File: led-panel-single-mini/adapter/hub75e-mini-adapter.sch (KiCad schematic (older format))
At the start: 2 parts, among them J1 Conn_02x08_Odd_Even, J2 Conn_02x08_Odd_Even

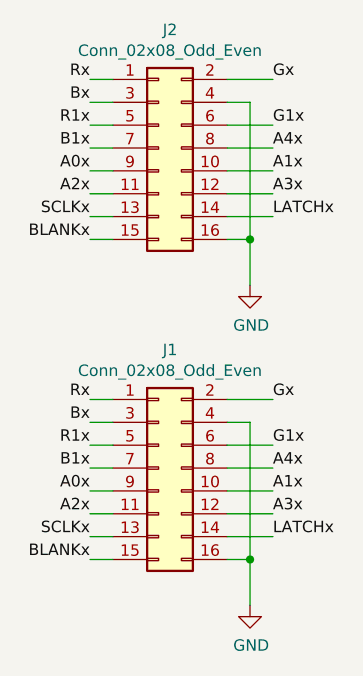
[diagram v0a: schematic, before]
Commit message: Corrected spacing and legend of the small led panel connector adapter.
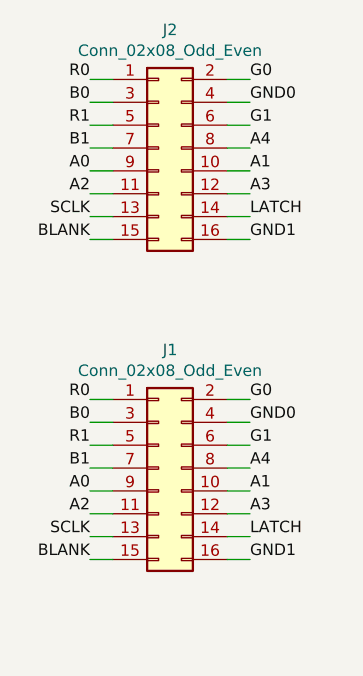
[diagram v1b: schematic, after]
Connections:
- net A0x renamed A0
- net A1x renamed A1
- net A2x renamed A2
- net A3x renamed A3
- net A4x renamed A4
- net B1x renamed B1
- net BLANKx renamed BLANK
- net Bx renamed B0
- net G1x renamed G1
- net GND renamed GND0
- net GND0: no longer J1.16 (Pin_16), J2.16 (Pin_16)
- net Gx renamed G0
- net LATCHx renamed LATCH
- net R1x renamed R1
- net Rx renamed R0
- net SCLKx renamed SCLK
- new net GND1: J1.16 (Pin_16), J2.16 (Pin_16)
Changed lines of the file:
@@
 EESchema Schematic File Version 4
 LIBS:hub75e-mini-adapter-cache
-EELAYER 26 0
+EELAYER 29 0
 EELAYER END
 $Descr A4 11693 8268
@@
 Title "HUB75E Mini Adapter"
 Date ""
-Rev "V1.0a"
+Rev "V1.0b"
 Comp "1BitSquared"
 Comment1 "2018-2019 (C) 1BitSquared <info@1bitsquared.com>"
@@
 	5500 3000 5400 3000
 Text Label 5400 2800 2    50   ~ 0
-Rx
-Text Label 6200 2800 0    50   ~ 0
-Gx
+R0
+Text Label 6100 2800 0    50   ~ 0
+G0
 Text Label 5400 2900 2    50   ~ 0
-Bx
+B0
 Text Label 5400 3000 2    50   ~ 0
-R1x
-Text Label 6200 3000 0    50   ~ 0
-G1x
+R1
+Text Label 6100 3000 0    50   ~ 0
+G1
 Text Label 5400 3100 2    50   ~ 0
-B1x
+B1
 Text Label 5400 3200 2    50   ~ 0
-A0x
-Text Label 6200 3200 0    50   ~ 0
-A1x
+A0
+Text Label 6100 3200 0    50   ~ 0
+A1
 Text Label 5400 3300 2    50   ~ 0
-A2x
-Text Label 6200 3300 0    50   ~ 0
-A3x
+A2
+Text Label 6100 3300 0    50   ~ 0
+A3
 Text Label 5400 3400 2    50   ~ 0
-SCLKx
-Text Label 6200 3400 0    50   ~ 0
-LATCHx
+SCLK
+Text Label 6100 3400 0    50   ~ 0
+LATCH
 Text Label 5400 3500 2    50   ~ 0
-BLANKx
-Text Label 6200 3100 0    50   ~ 0
-A4x
+BLANK
+Text Label 6100 3100 0    50   ~ 0
+A4
 Wire Wire Line
 	5400 3100 5500 3100
@@
 	5400 3500 5500 3500
 Wire Wire Line
-	6000 2800 6200 2800
+	6000 2800 6100 2800
 Wire Wire Line
-	6000 3000 6200 3000
+	6000 3000 6100 3000
 Wire Wire Line
-	6000 3100 6200 3100
+	6000 3100 6100 3100
 Wire Wire Line
-	6000 3200 6200 3200
+	6000 3200 6100 3200
 Wire Wire Line
-	6000 3300 6200 3300
+	6000 3300 6100 3300
 Wire Wire Line
-	6000 3400 6200 3400
+	6000 3400 6100 3400
 Wire Wire Line
 	6000 2900 6100 2900
-Wire Wire Line
-	6100 2900 6100 3500
-Wire Wire Line
-	6100 3500 6100 3700
-Connection ~ 6100 3500
-$Comp
-L power:GND #PWR03
-U 1 1 5C8CBF07
-P 6100 3700
-F 0 "#PWR03" H 6100 3450 50  0001 C CNN
-F 1 "GND" H 6105 3524 50  0000 C CNN
-F 2 "" H 6100 3700 50  0001 C CNN
-F 3 "" H 6100 3700 50  0001 C CNN
-	1    6100 3700
-	1    0    0    -1
-$EndComp
 $Comp
 L Connector_Generic:Conn_02x08_Odd_Even J1
@@
 	5500 4400 5400 4400
 Text Label 5400 4200 2    50   ~ 0
-Rx
-Text Label 6200 4200 0    50   ~ 0
-Gx
+R0
+Text Label 6100 4200 0    50   ~ 0
+G0
 Text Label 5400 4300 2    50   ~ 0
-Bx
+B0
 Text Label 5400 4400 2    50   ~ 0
-R1x
-Text Label 6200 4400 0    50   ~ 0
-G1x
+R1
+Text Label 6100 4400 0    50   ~ 0
+G1
 Text Label 5400 4500 2    50   ~ 0
-B1x
+B1
 Text Label 5400 4600 2    50   ~ 0
-A0x
-Text Label 6200 4600 0    50   ~ 0
-A1x
+A0
+Text Label 6100 4600 0    50   ~ 0
+A1
 Text Label 5400 4700 2    50   ~ 0
-A2x
-Text Label 6200 4700 0    50   ~ 0
-A3x
+A2
+Text Label 6100 4700 0    50   ~ 0
+A3
 Text Label 5400 4800 2    50   ~ 0
-SCLKx
-Text Label 6200 4800 0    50   ~ 0
-LATCHx
+SCLK
+Text Label 6100 4800 0    50   ~ 0
+LATCH
 Text Label 5400 4900 2    50   ~ 0
-BLANKx
-Text Label 6200 4500 0    50   ~ 0
-A4x
+BLANK
+Text Label 6100 4500 0    50   ~ 0
+A4
 Wire Wire Line
 	5400 4500 5500 4500
@@
 	5400 4900 5500 4900
 Wire Wire Line
-	6000 4200 6200 4200
+	6000 4200 6100 4200
 Wire Wire Line
-	6000 4400 6200 4400
+	6000 4400 6100 4400
 Wire Wire Line
-	6000 4500 6200 4500
+	6000 4500 6100 4500
 Wire Wire Line
-	6000 4600 6200 4600
+	6000 4600 6100 4600
 Wire Wire Line
-	6000 4700 6200 4700
+	6000 4700 6100 4700
 Wire Wire Line
-	6000 4800 6200 4800
+	6000 4800 6100 4800
 Wire Wire Line
 	6000 4300 6100 4300
-Wire Wire Line
-	6100 4300 6100 4900
-Wire Wire Line
-	6100 4900 6100 5100
-Connection ~ 6100 4900
-$Comp
-L power:GND #PWR0101
-U 1 1 5C5ACFE9
-P 6100 5100
-F 0 "#PWR0101" H 6100 4850 50  0001 C CNN
-F 1 "GND" H 6105 4924 50  0000 C CNN
-F 2 "" H 6100 5100 50  0001 C CNN
-F 3 "" H 6100 5100 50  0001 C CNN
-	1    6100 5100
-	1    0    0    -1
-$EndComp
+Text Label 6100 2900 0    50   ~ 0
+GND0
+Text Label 6100 3500 0    50   ~ 0
+GND1
+Text Label 6100 4300 0    50   ~ 0
+GND0
+Text Label 6100 4900 0    50   ~ 0
+GND1
 $EndSCHEMATC
